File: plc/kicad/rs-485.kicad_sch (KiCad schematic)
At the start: 10 parts, among them CN3 DB2ERC-5.08-4P, SW1 MSK12C02, U11 THVD1450DR

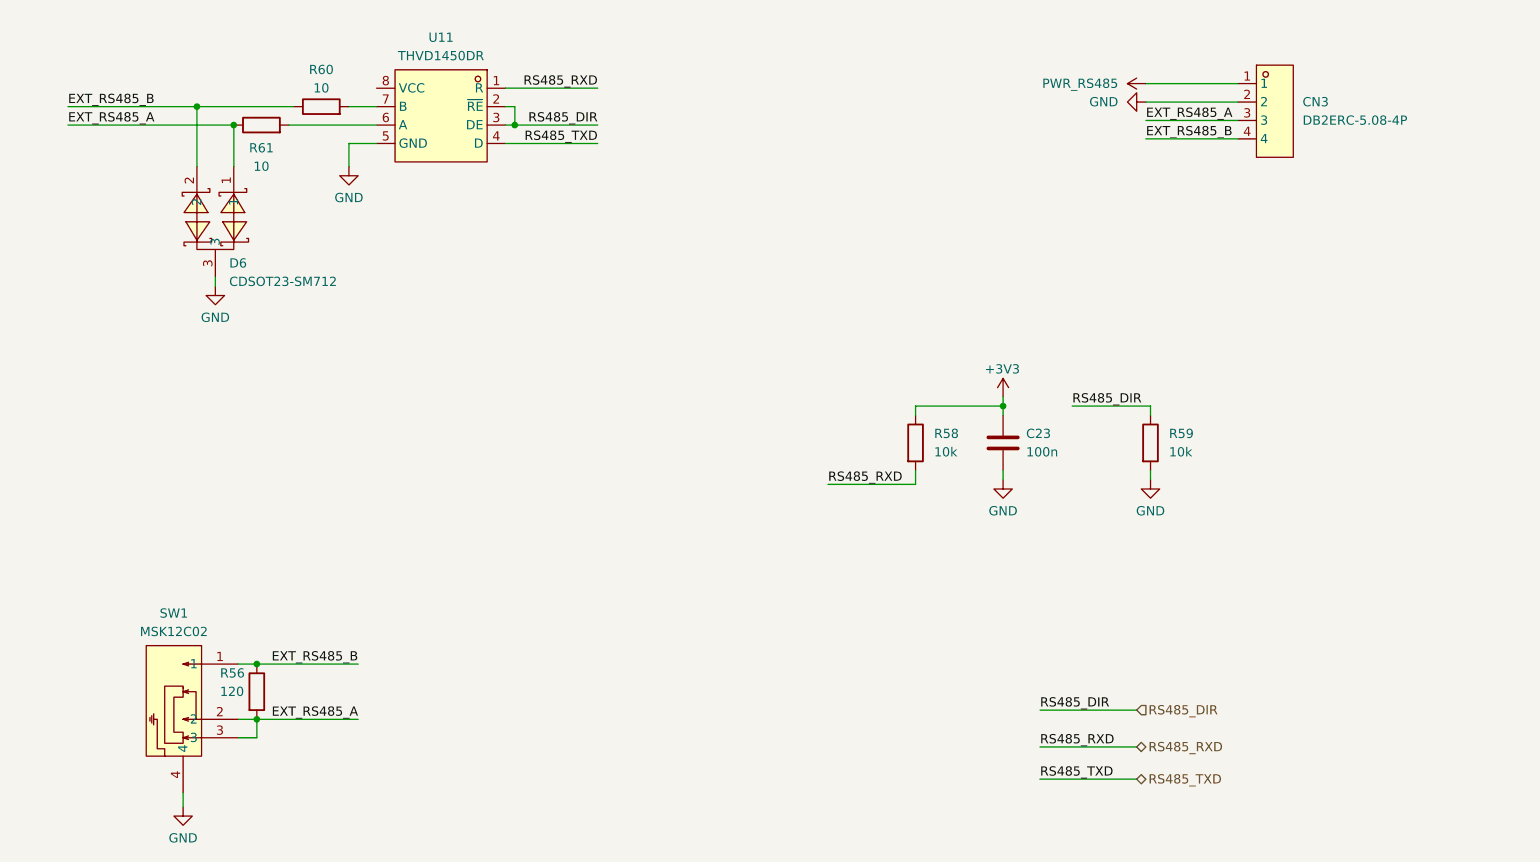
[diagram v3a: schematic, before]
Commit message: Added CP2102N bridge
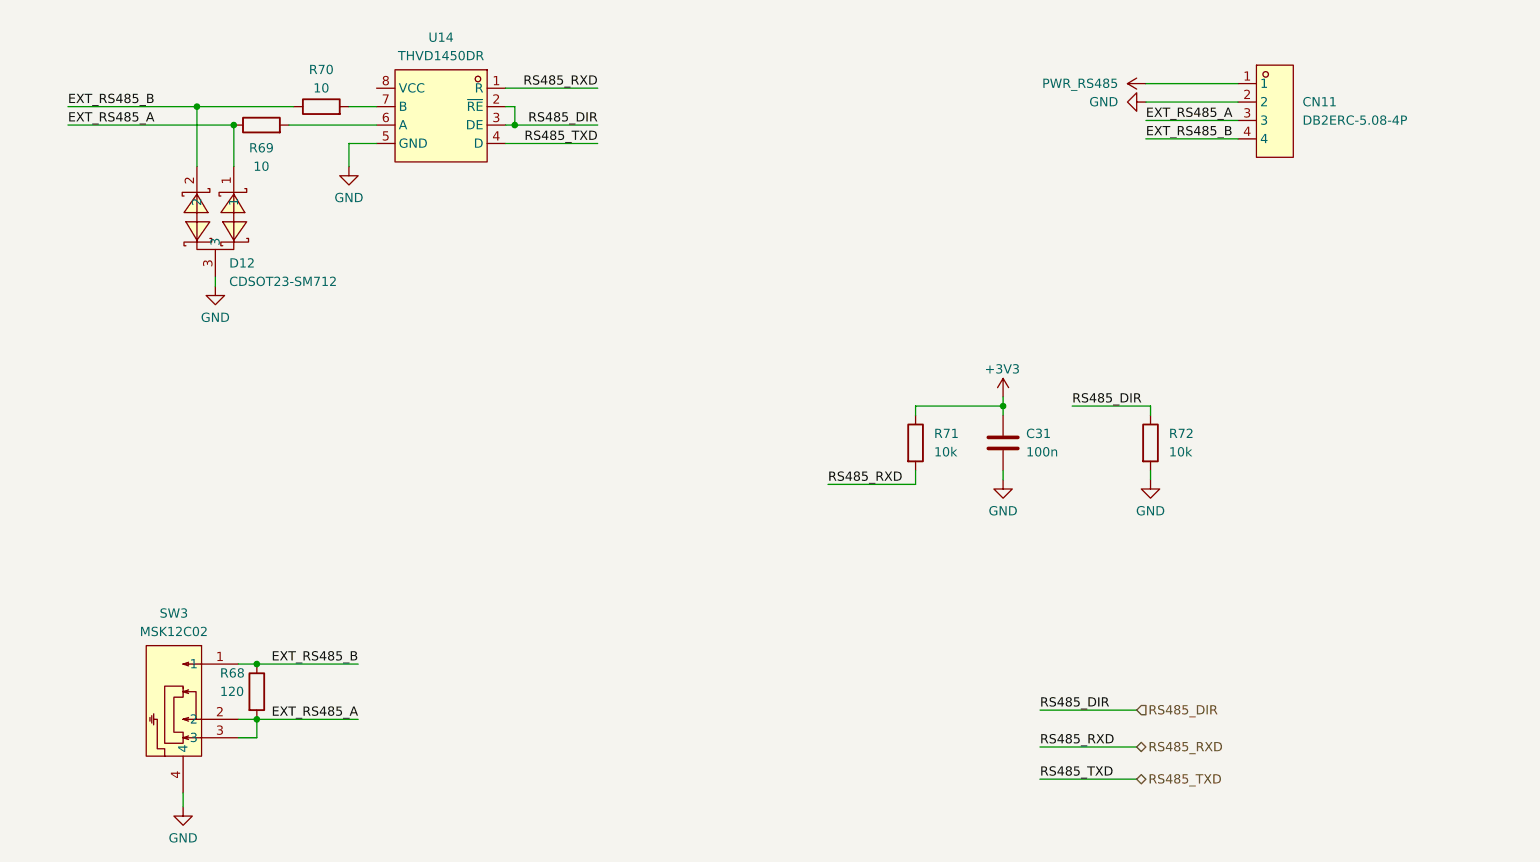
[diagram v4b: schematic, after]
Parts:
- renumbered C23 to C31, CN3 to CN11, D6 to D12, R56 to R68, R61 to R69, R60 to R70, R58 to R71, R59 to R72, SW1 to SW3, U11 to U14
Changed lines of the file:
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@@
 		(dnp no)
 		(fields_autoplaced yes)
-		(property "Reference" "#PWR0124"
+		(property "Reference" "#PWR0142"
 			(at 192.405 121.92 0)
 			(hide yes)
@@
 			(project "LibrePLC32"
 				(path "/ef4c1a27-85a3-413a-9f93-a41c4f97eee5/58fa1ecb-ea1c-4a70-bb90-31ff9b441562"
-					(reference "#PWR0124")
+					(reference "#PWR0142")
 					(unit 1)
 				)
@@
 		(dnp no)
 		(fields_autoplaced yes)
-		(property "Reference" "#PWR0120"
+		(property "Reference" "#PWR0137"
 			(at 81.915 78.74 0)
 			(hide yes)
@@
 			(project "LibrePLC32"
 				(path "/ef4c1a27-85a3-413a-9f93-a41c4f97eee5/58fa1ecb-ea1c-4a70-bb90-31ff9b441562"
-					(reference "#PWR0120")
+					(reference "#PWR0137")
 					(unit 1)
 				)
@@
 		(dnp no)
 		(fields_autoplaced yes)
-		(property "Reference" "R59"
+		(property "Reference" "R72"
 			(at 194.945 109.2199 0)
 			(show_name no)
@@
 			(project "LibrePLC32"
 				(path "/ef4c1a27-85a3-413a-9f93-a41c4f97eee5/58fa1ecb-ea1c-4a70-bb90-31ff9b441562"
-					(reference "R59")
+					(reference "R72")
 					(unit 1)
 				)
@@
 		(in_pos_files yes)
 		(dnp no)
-		(property "Reference" "D6"
+		(property "Reference" "D12"
 			(at 65.405 85.725 0)
 			(show_name no)
@@
 			(project "LibrePLC32"
 				(path "/ef4c1a27-85a3-413a-9f93-a41c4f97eee5/58fa1ecb-ea1c-4a70-bb90-31ff9b441562"
-					(reference "D6")
+					(reference "D12")
 					(unit 1)
 				)
@@
 		(in_pos_files yes)
 		(dnp no)
-		(property "Reference" "R56"
+		(property "Reference" "R68"
 			(at 64.135 142.24 0)
 			(show_name no)
@@
 			(project "LibrePLC32"
 				(path "/ef4c1a27-85a3-413a-9f93-a41c4f97eee5/58fa1ecb-ea1c-4a70-bb90-31ff9b441562"
-					(reference "R56")
+					(reference "R68")
 					(unit 1)
 				)
@@
 		(dnp no)
 		(fields_autoplaced yes)
-		(property "Reference" "SW1"
+		(property "Reference" "SW3"
 			(at 57.785 133.985 90)
 			(show_name no)
@@
 			(project "LibrePLC32"
 				(path "/ef4c1a27-85a3-413a-9f93-a41c4f97eee5/58fa1ecb-ea1c-4a70-bb90-31ff9b441562"
-					(reference "SW1")
+					(reference "SW3")
 					(unit 1)
 				)
@@
 		(in_pos_files yes)
 		(dnp no)
-		(property "Reference" "#PWR0122"
+		(property "Reference" "#PWR0138"
 			(at 172.085 107.95 0)
 			(hide yes)
@@
 			(project "LibrePLC32"
 				(path "/ef4c1a27-85a3-413a-9f93-a41c4f97eee5/58fa1ecb-ea1c-4a70-bb90-31ff9b441562"
-					(reference "#PWR0122")
+					(reference "#PWR0138")
 					(unit 1)
 				)
@@
 		(in_pos_files yes)
 		(dnp no)
-		(property "Reference" "R60"
+		(property "Reference" "R70"
 			(at 78.105 59.055 90)
 			(show_name no)
@@
 			(project "LibrePLC32"
 				(path "/ef4c1a27-85a3-413a-9f93-a41c4f97eee5/58fa1ecb-ea1c-4a70-bb90-31ff9b441562"
-					(reference "R60")
+					(reference "R70")
 					(unit 1)
 				)
@@
 		(dnp no)
 		(fields_autoplaced yes)
-		(property "Reference" "#PWR0141"
+		(property "Reference" "#PWR0140"
 			(at 195.58 60.96 0)
 			(hide yes)
@@
 			(project "LibrePLC32"
 				(path "/ef4c1a27-85a3-413a-9f93-a41c4f97eee5/58fa1ecb-ea1c-4a70-bb90-31ff9b441562"
-					(reference "#PWR0141")
+					(reference "#PWR0140")
 					(unit 1)
 				)
@@
 		(dnp no)
 		(fields_autoplaced yes)
-		(property "Reference" "CN3"
+		(property "Reference" "CN11"
 			(at 213.36 63.4999 0)
 			(show_name no)
@@
 			(project "LibrePLC32"
 				(path "/ef4c1a27-85a3-413a-9f93-a41c4f97eee5/58fa1ecb-ea1c-4a70-bb90-31ff9b441562"
-					(reference "CN3")
+					(reference "CN11")
 					(unit 1)
 				)
@@
 		(dnp no)
 		(fields_autoplaced yes)
-		(property "Reference" "C23"
+		(property "Reference" "C31"
 			(at 175.26 109.2199 0)
 			(show_name no)
@@
 			(project "LibrePLC32"
 				(path "/ef4c1a27-85a3-413a-9f93-a41c4f97eee5/58fa1ecb-ea1c-4a70-bb90-31ff9b441562"
-					(reference "C23")
+					(reference "C31")
 					(unit 1)
 				)
@@
 		(dnp no)
 		(fields_autoplaced yes)
-		(property "Reference" "#PWR0123"
+		(property "Reference" "#PWR0136"
 			(at 63.5 95.25 0)
 			(hide yes)
@@
 			(project "LibrePLC32"
 				(path "/ef4c1a27-85a3-413a-9f93-a41c4f97eee5/58fa1ecb-ea1c-4a70-bb90-31ff9b441562"
-					(reference "#PWR0123")
+					(reference "#PWR0136")
 					(unit 1)
 				)
@@
 		(in_pos_files yes)
 		(dnp no)
-		(property "Reference" "R61"
+		(property "Reference" "R69"
 			(at 69.85 69.85 90)
 			(show_name no)
@@
 			(project "LibrePLC32"
 				(path "/ef4c1a27-85a3-413a-9f93-a41c4f97eee5/58fa1ecb-ea1c-4a70-bb90-31ff9b441562"
-					(reference "R61")
+					(reference "R69")
 					(unit 1)
 				)
@@
 		(in_pos_files yes)
 		(dnp no)
-		(property "Reference" "U11"
+		(property "Reference" "U14"
 			(at 94.615 54.61 0)
 			(show_name no)
@@
 			(project "LibrePLC32"
 				(path "/ef4c1a27-85a3-413a-9f93-a41c4f97eee5/58fa1ecb-ea1c-4a70-bb90-31ff9b441562"
-					(reference "U11")
+					(reference "U14")
 					(unit 1)
 				)
@@
 		(dnp no)
 		(fields_autoplaced yes)
-		(property "Reference" "#PWR0125"
+		(property "Reference" "#PWR0135"
 			(at 59.055 167.005 0)
 			(hide yes)
@@
 			(project "LibrePLC32"
 				(path "/ef4c1a27-85a3-413a-9f93-a41c4f97eee5/58fa1ecb-ea1c-4a70-bb90-31ff9b441562"
-					(reference "#PWR0125")
+					(reference "#PWR0135")
 					(unit 1)
 				)
@@
 		(dnp no)
 		(fields_autoplaced yes)
-		(property "Reference" "R58"
+		(property "Reference" "R71"
 			(at 162.56 109.2199 0)
 			(show_name no)
@@
 			(project "LibrePLC32"
 				(path "/ef4c1a27-85a3-413a-9f93-a41c4f97eee5/58fa1ecb-ea1c-4a70-bb90-31ff9b441562"
-					(reference "R58")
+					(reference "R71")
 					(unit 1)
 				)
@@
 		(dnp no)
 		(fields_autoplaced yes)
-		(property "Reference" "#PWR0126"
+		(property "Reference" "#PWR0141"
 			(at 185.42 63.5 0)
 			(hide yes)
@@
 			(project "LibrePLC32"
 				(path "/ef4c1a27-85a3-413a-9f93-a41c4f97eee5/58fa1ecb-ea1c-4a70-bb90-31ff9b441562"
-					(reference "#PWR0126")
+					(reference "#PWR0141")
 					(unit 1)
 				)
@@
 		(dnp no)
 		(fields_autoplaced yes)
-		(property "Reference" "#PWR0121"
+		(property "Reference" "#PWR0139"
 			(at 172.085 121.92 0)
 			(hide yes)
@@
 			(project "LibrePLC32"
 				(path "/ef4c1a27-85a3-413a-9f93-a41c4f97eee5/58fa1ecb-ea1c-4a70-bb90-31ff9b441562"
-					(reference "#PWR0121")
-					(unit 1)
-				)
+					(reference "#PWR0139")
+					(unit 1)
+				)

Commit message: Added 3.3V regulator
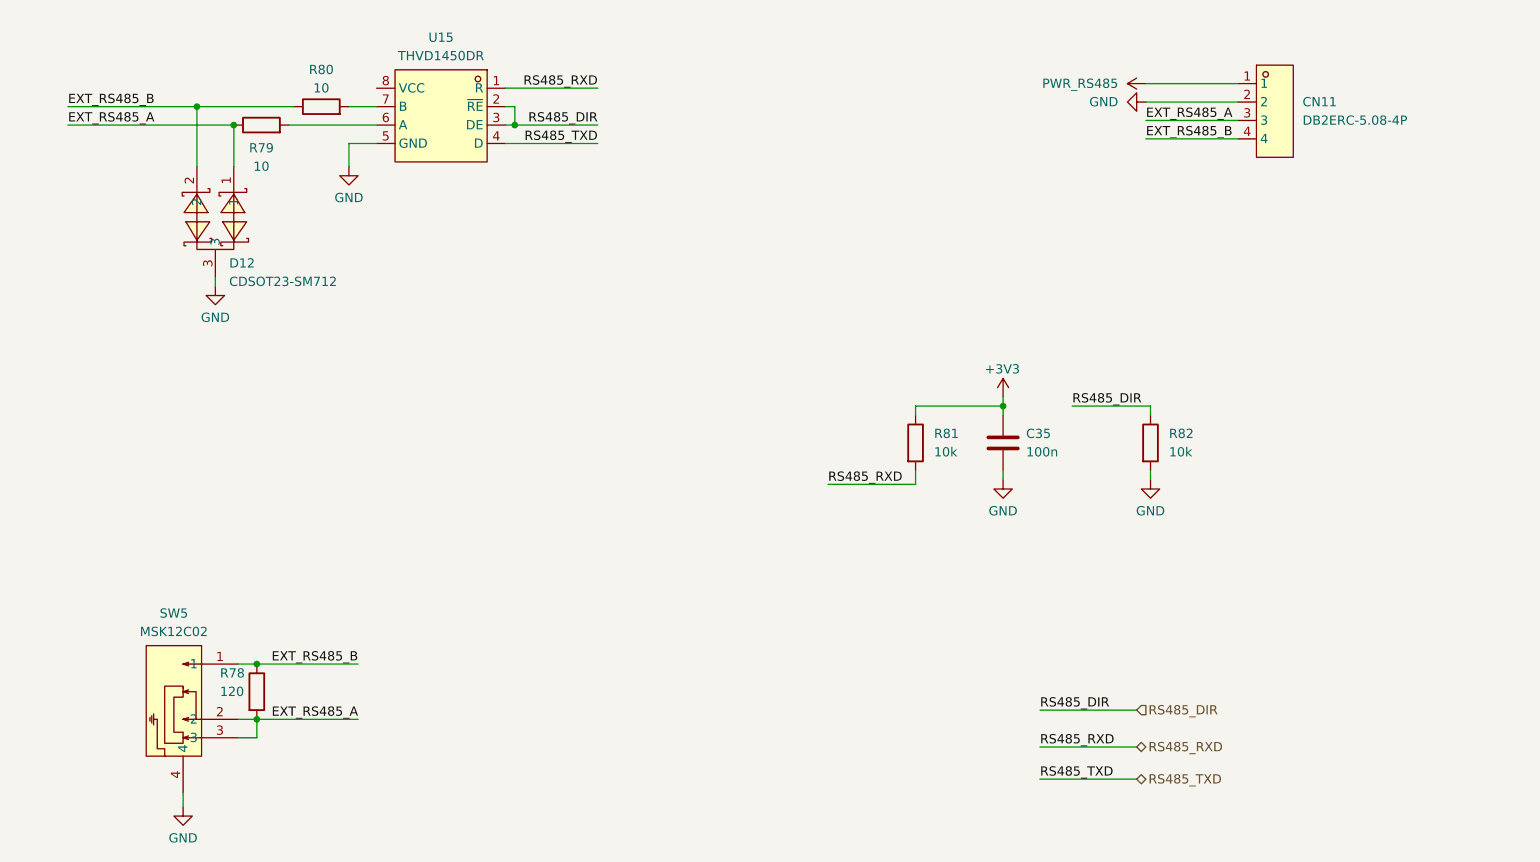
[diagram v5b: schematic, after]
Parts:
- renumbered C31 to C35, R68 to R78, R69 to R79, R70 to R80, R71 to R81, R72 to R82, SW3 to SW5, U14 to U15
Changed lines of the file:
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@@
 		(dnp no)
 		(fields_autoplaced yes)
-		(property "Reference" "#PWR0142"
+		(property "Reference" "#PWR0171"
 			(at 192.405 121.92 0)
 			(hide yes)
@@
 			(project "LibrePLC32"
 				(path "/ef4c1a27-85a3-413a-9f93-a41c4f97eee5/58fa1ecb-ea1c-4a70-bb90-31ff9b441562"
-					(reference "#PWR0142")
+					(reference "#PWR0171")
 					(unit 1)
 				)
@@
 		(dnp no)
 		(fields_autoplaced yes)
-		(property "Reference" "#PWR0137"
+		(property "Reference" "#PWR0166"
 			(at 81.915 78.74 0)
 			(hide yes)
@@
 			(project "LibrePLC32"
 				(path "/ef4c1a27-85a3-413a-9f93-a41c4f97eee5/58fa1ecb-ea1c-4a70-bb90-31ff9b441562"
-					(reference "#PWR0137")
+					(reference "#PWR0166")
 					(unit 1)
 				)
@@
 		(dnp no)
 		(fields_autoplaced yes)
-		(property "Reference" "R72"
+		(property "Reference" "R82"
 			(at 194.945 109.2199 0)
 			(show_name no)
@@
 			(project "LibrePLC32"
 				(path "/ef4c1a27-85a3-413a-9f93-a41c4f97eee5/58fa1ecb-ea1c-4a70-bb90-31ff9b441562"
-					(reference "R72")
+					(reference "R82")
 					(unit 1)
 				)
@@
 		(in_pos_files yes)
 		(dnp no)
-		(property "Reference" "R68"
+		(property "Reference" "R78"
 			(at 64.135 142.24 0)
 			(show_name no)
@@
 			(project "LibrePLC32"
 				(path "/ef4c1a27-85a3-413a-9f93-a41c4f97eee5/58fa1ecb-ea1c-4a70-bb90-31ff9b441562"
-					(reference "R68")
+					(reference "R78")
 					(unit 1)
 				)
@@
 		(dnp no)
 		(fields_autoplaced yes)
-		(property "Reference" "SW3"
+		(property "Reference" "SW5"
 			(at 57.785 133.985 90)
 			(show_name no)
@@
 			(project "LibrePLC32"
 				(path "/ef4c1a27-85a3-413a-9f93-a41c4f97eee5/58fa1ecb-ea1c-4a70-bb90-31ff9b441562"
-					(reference "SW3")
+					(reference "SW5")
 					(unit 1)
 				)
@@
 		(in_pos_files yes)
 		(dnp no)
-		(property "Reference" "#PWR0138"
+		(property "Reference" "#PWR0167"
 			(at 172.085 107.95 0)
 			(hide yes)
@@
 			(project "LibrePLC32"
 				(path "/ef4c1a27-85a3-413a-9f93-a41c4f97eee5/58fa1ecb-ea1c-4a70-bb90-31ff9b441562"
-					(reference "#PWR0138")
+					(reference "#PWR0167")
 					(unit 1)
 				)
@@
 		(in_pos_files yes)
 		(dnp no)
-		(property "Reference" "R70"
+		(property "Reference" "R80"
 			(at 78.105 59.055 90)
 			(show_name no)
@@
 			(project "LibrePLC32"
 				(path "/ef4c1a27-85a3-413a-9f93-a41c4f97eee5/58fa1ecb-ea1c-4a70-bb90-31ff9b441562"
-					(reference "R70")
+					(reference "R80")
 					(unit 1)
 				)
@@
 		(dnp no)
 		(fields_autoplaced yes)
-		(property "Reference" "#PWR0140"
+		(property "Reference" "#PWR0169"
 			(at 195.58 60.96 0)
 			(hide yes)
@@
 			(project "LibrePLC32"
 				(path "/ef4c1a27-85a3-413a-9f93-a41c4f97eee5/58fa1ecb-ea1c-4a70-bb90-31ff9b441562"
-					(reference "#PWR0140")
+					(reference "#PWR0169")
 					(unit 1)
 				)
@@
 		(dnp no)
 		(fields_autoplaced yes)
-		(property "Reference" "C31"
+		(property "Reference" "C35"
 			(at 175.26 109.2199 0)
 			(show_name no)
@@
 			(project "LibrePLC32"
 				(path "/ef4c1a27-85a3-413a-9f93-a41c4f97eee5/58fa1ecb-ea1c-4a70-bb90-31ff9b441562"
-					(reference "C31")
+					(reference "C35")
 					(unit 1)
 				)
@@
 		(dnp no)
 		(fields_autoplaced yes)
-		(property "Reference" "#PWR0136"
+		(property "Reference" "#PWR0165"
 			(at 63.5 95.25 0)
 			(hide yes)
@@
 			(project "LibrePLC32"
 				(path "/ef4c1a27-85a3-413a-9f93-a41c4f97eee5/58fa1ecb-ea1c-4a70-bb90-31ff9b441562"
-					(reference "#PWR0136")
+					(reference "#PWR0165")
 					(unit 1)
 				)
@@
 		(in_pos_files yes)
 		(dnp no)
-		(property "Reference" "R69"
+		(property "Reference" "R79"
 			(at 69.85 69.85 90)
 			(show_name no)
@@
 			(project "LibrePLC32"
 				(path "/ef4c1a27-85a3-413a-9f93-a41c4f97eee5/58fa1ecb-ea1c-4a70-bb90-31ff9b441562"
-					(reference "R69")
+					(reference "R79")
 					(unit 1)
 				)
@@
 		(in_pos_files yes)
 		(dnp no)
-		(property "Reference" "U14"
+		(property "Reference" "U15"
 			(at 94.615 54.61 0)
 			(show_name no)
@@
 			(project "LibrePLC32"
 				(path "/ef4c1a27-85a3-413a-9f93-a41c4f97eee5/58fa1ecb-ea1c-4a70-bb90-31ff9b441562"
-					(reference "U14")
+					(reference "U15")
 					(unit 1)
 				)
@@
 		(dnp no)
 		(fields_autoplaced yes)
-		(property "Reference" "#PWR0135"
+		(property "Reference" "#PWR0164"
 			(at 59.055 167.005 0)
 			(hide yes)
@@
 			(project "LibrePLC32"
 				(path "/ef4c1a27-85a3-413a-9f93-a41c4f97eee5/58fa1ecb-ea1c-4a70-bb90-31ff9b441562"
-					(reference "#PWR0135")
+					(reference "#PWR0164")
 					(unit 1)
 				)
@@
 		(dnp no)
 		(fields_autoplaced yes)
-		(property "Reference" "R71"
+		(property "Reference" "R81"
 			(at 162.56 109.2199 0)
 			(show_name no)
@@
 			(project "LibrePLC32"
 				(path "/ef4c1a27-85a3-413a-9f93-a41c4f97eee5/58fa1ecb-ea1c-4a70-bb90-31ff9b441562"
-					(reference "R71")
+					(reference "R81")
 					(unit 1)
 				)
@@
 		(dnp no)
 		(fields_autoplaced yes)
-		(property "Reference" "#PWR0141"
+		(property "Reference" "#PWR0170"
 			(at 185.42 63.5 0)
 			(hide yes)
@@
 			(project "LibrePLC32"
 				(path "/ef4c1a27-85a3-413a-9f93-a41c4f97eee5/58fa1ecb-ea1c-4a70-bb90-31ff9b441562"
-					(reference "#PWR0141")
+					(reference "#PWR0170")
 					(unit 1)
 				)
@@
 		(dnp no)
 		(fields_autoplaced yes)
-		(property "Reference" "#PWR0139"
+		(property "Reference" "#PWR0168"
 			(at 172.085 121.92 0)
 			(hide yes)
@@
 			(project "LibrePLC32"
 				(path "/ef4c1a27-85a3-413a-9f93-a41c4f97eee5/58fa1ecb-ea1c-4a70-bb90-31ff9b441562"
-					(reference "#PWR0139")
-					(unit 1)
-				)
+					(reference "#PWR0168")
+					(unit 1)
+				)
